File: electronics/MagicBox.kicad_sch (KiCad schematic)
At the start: 32 parts, among them SW1 SW_Push, SW2 SW_Push, SW3 SW_Push, SW4 SW_Push, SW5 SW_Push, SW6 SW_DPST_x2, SW7 RotaryEncoder_Switch, U1 ESP32-WROOM-32, U2 L7805

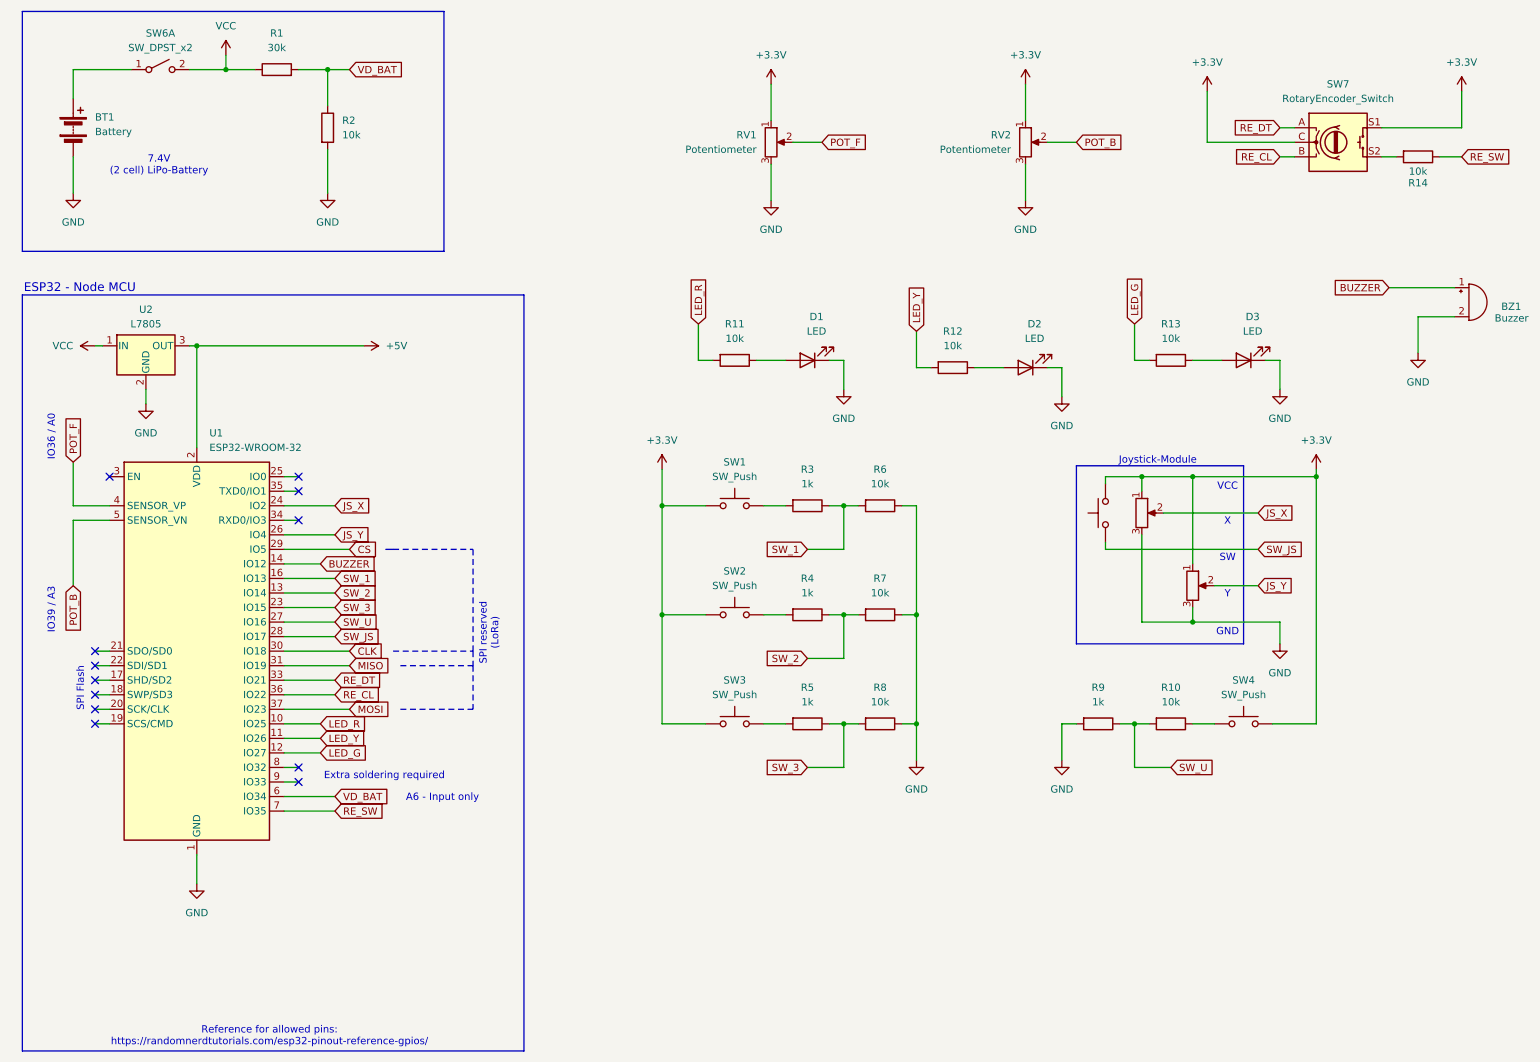
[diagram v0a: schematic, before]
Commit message: updated schematics
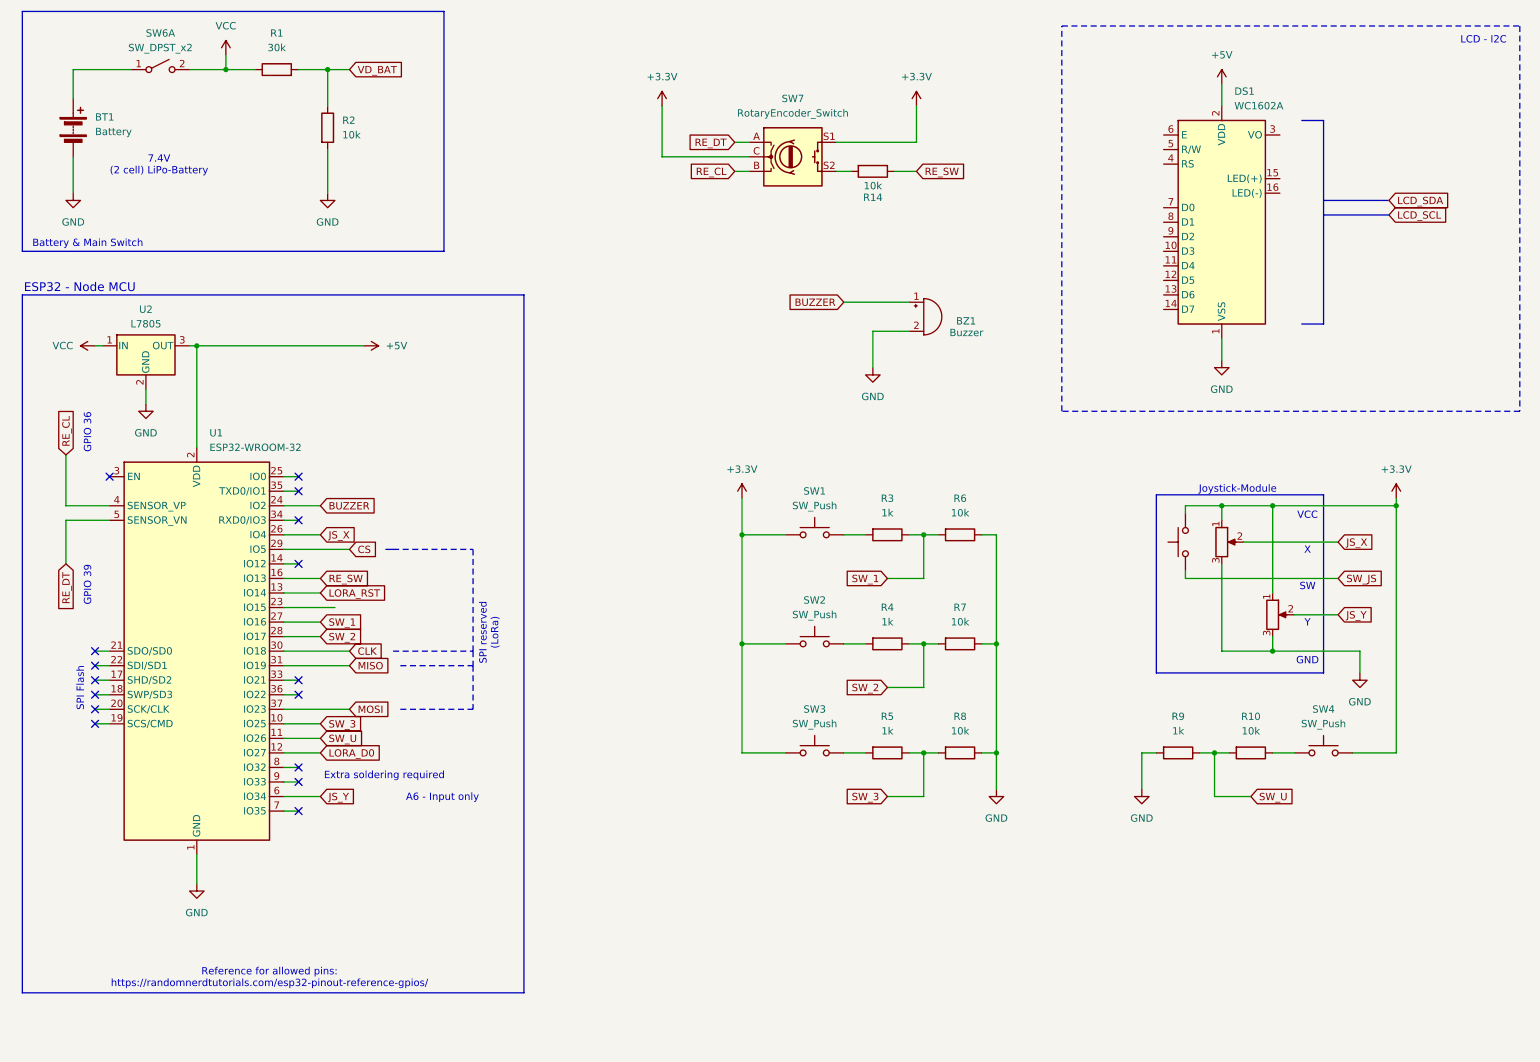
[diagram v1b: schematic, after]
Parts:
- removed D1, D2, D3: LED, symbol Device:LED
- removed R11, R12, R13: 10k, symbol Device:R
- removed RV1, RV2: Potentiometer, symbol Device:R_Potentiometer
- added DS1: WC1602A, Display:WC1602A, symbol Display_Character:WC1602A
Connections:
- net LED_R is gone; now on net SW_3: U1.10 (IO25)
- net LED_Y is gone; now on net SW_U: U1.11 (IO26)
- net POT_B is gone; now on net RE_DT: U1.5 (SENSOR_VN)
- net POT_F is gone; now on net RE_CL: U1.4 (SENSOR_VP)
- net +5V: now also DS1.2 (VDD)
- net BUZZER: now also U1.24 (IO2); no longer U1.14 (IO12)
- net GND: now also DS1.1 (VSS)
- net JS_X: now also U1.26 (IO4); no longer U1.24 (IO2)
- net JS_Y: now also U1.6 (IO34); no longer U1.26 (IO4)
- net RE_CL: no longer U1.36 (IO22)
- net RE_DT: no longer U1.33 (IO21)
- net RE_SW: now also U1.16 (IO13); no longer U1.7 (IO35)
- net SW_1: now also U1.27 (IO16); no longer U1.16 (IO13)
- net SW_2: now also U1.28 (IO17); no longer U1.13 (IO14)
- net SW_3: no longer U1.23 (IO15)
- net SW_JS: no longer U1.28 (IO17)
- net SW_U: no longer U1.27 (IO16)
- net VD_BAT: no longer U1.6 (IO34)
- net LED_G renamed LORA_D0
- new net LORA_RST: U1.13 (IO14)
- no-connect marks 12 -> 16
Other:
- note added: "Battery & Main Switch"
- note added: "GPIO 36"
- note added: "GPIO 39"
- note added: "LCD - I2C"
- note removed: "IO36 / A0"
- note removed: "IO39 / A3"
- company: Sy (Samuel Nösslböck) - CircleLab/CornerLab Inc. -> Sy (Samuel Nösslböck) - CornerLab Inc.
- title: SpellBox -> MagicBox
- moved on the sheet: BZ1, R10, R14, R3, R4, R5, R6, R7, R8, R9, SW1, SW2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
